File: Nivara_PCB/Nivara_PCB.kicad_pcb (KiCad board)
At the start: 2 copper layers, 102.2 x 83 mm, 20 parts, among them J1 NPN_IN, J10 PNP_OUT, J11 Analog_Out, J2 PNP_IN, J3 D_IN, J4 NPN_OUT, J5 RELAY, J6 RUN/STOP, J7 FUENTE, J8 RS485, J9 Analaog_In, U1 ESP32-S3-WROOM-1, U2 AP63203WU

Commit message: Actualización del pcb
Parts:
- C1: renamed from C3; value C_1206 -> 10uF
- moved C6 28.5 mm to (128.5, 78.7)
- moved R1 26.8 mm to (128.0, 71.3), turned to -90 degrees
- moved C1 13.8 mm to (107.0, 56.5), turned to 180 degrees
- moved C3 13.3 mm to (103.5, 60.0)
- moved C5 9.69 mm to (114.0, 60.0)
- moved C2 9.18 mm to (111.5, 60.0)
- moved U2 8.86 mm to (107.4, 60.0), turned to 180 degrees
- moved L1 3.08 mm to (107.0, 65.5), turned to 0 degrees
- renumbered C4 to C2, C2 to C3, C6 to C5, C1 to C6
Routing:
- net +3.3V: track 0.00 -> 11.8 mm
- net Net-(U2-SW): track 0.00 -> 11.6 mm
- net VCC: track 0.00 -> 10.8 mm
- net Net-(U2-BST): track 0.00 -> 2.73 mm
- net GND: vias 0 -> 17
- added copper zone on F.Cu, net GND

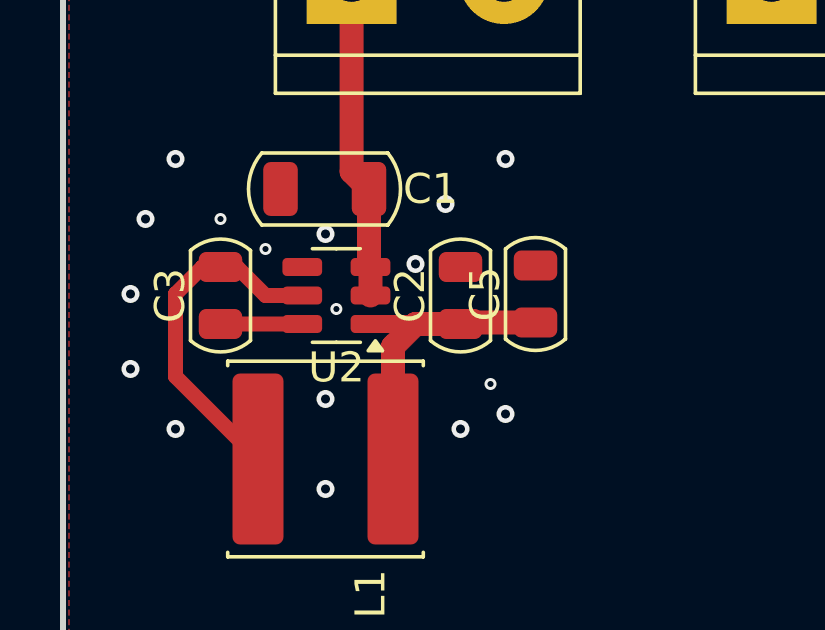
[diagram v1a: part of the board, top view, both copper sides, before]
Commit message: Fuente de 12V para activar optoacopladores y relés
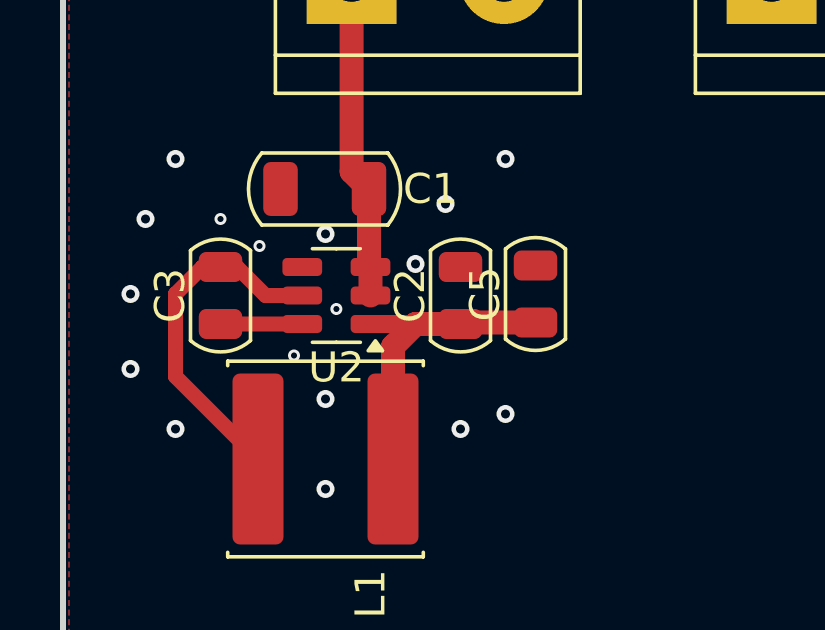
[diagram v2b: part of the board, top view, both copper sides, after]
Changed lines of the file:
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@@
 	)
 	(via
-		(at 112.55 63)
+		(at 106 62.05)
 		(size 0.4)
 		(drill 0.2)
@@
 	)
 	(via
-		(at 105.05 58.5)
+		(at 104.85 58.4)
 		(size 0.4)
 		(drill 0.2)

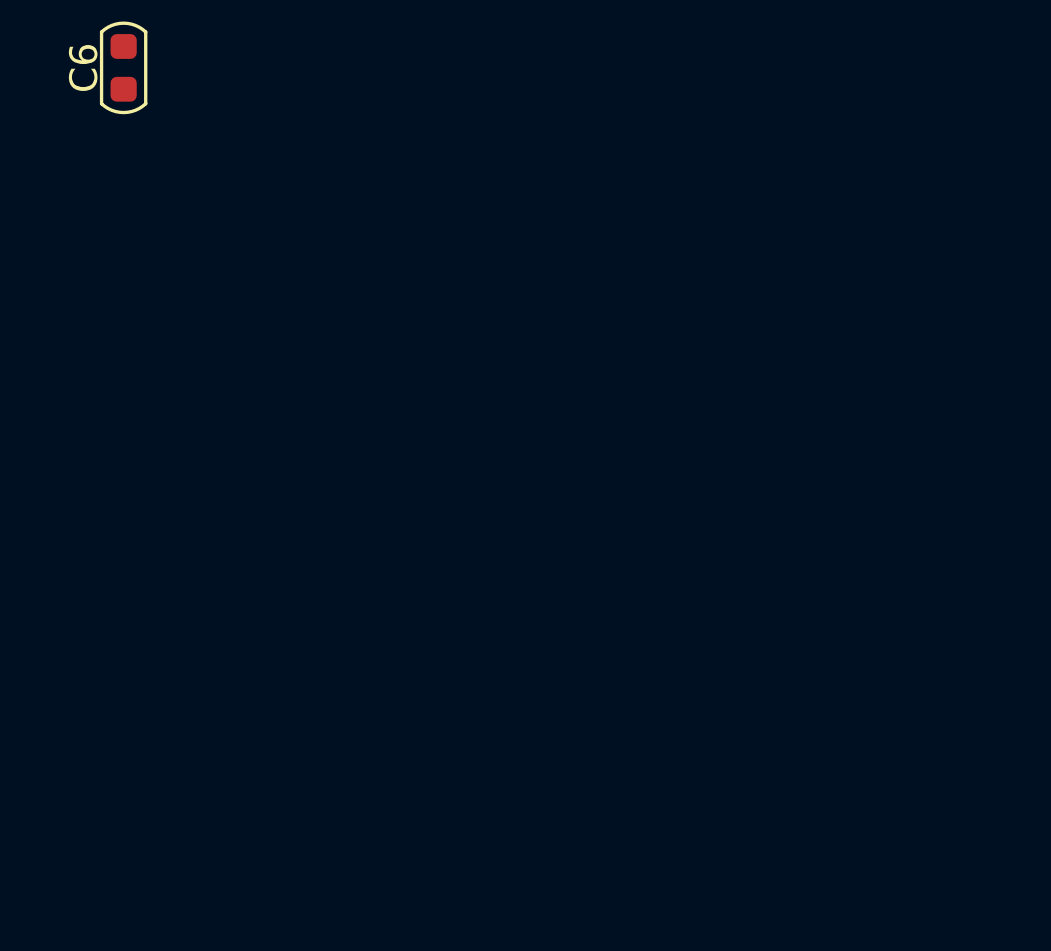
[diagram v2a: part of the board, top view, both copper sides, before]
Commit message: Cambio a fuente de 5V para utilizar reles HF49FD Es mejor utilizar una fuente de 5V para alimentar los reles y los periféricos en general, que 12V
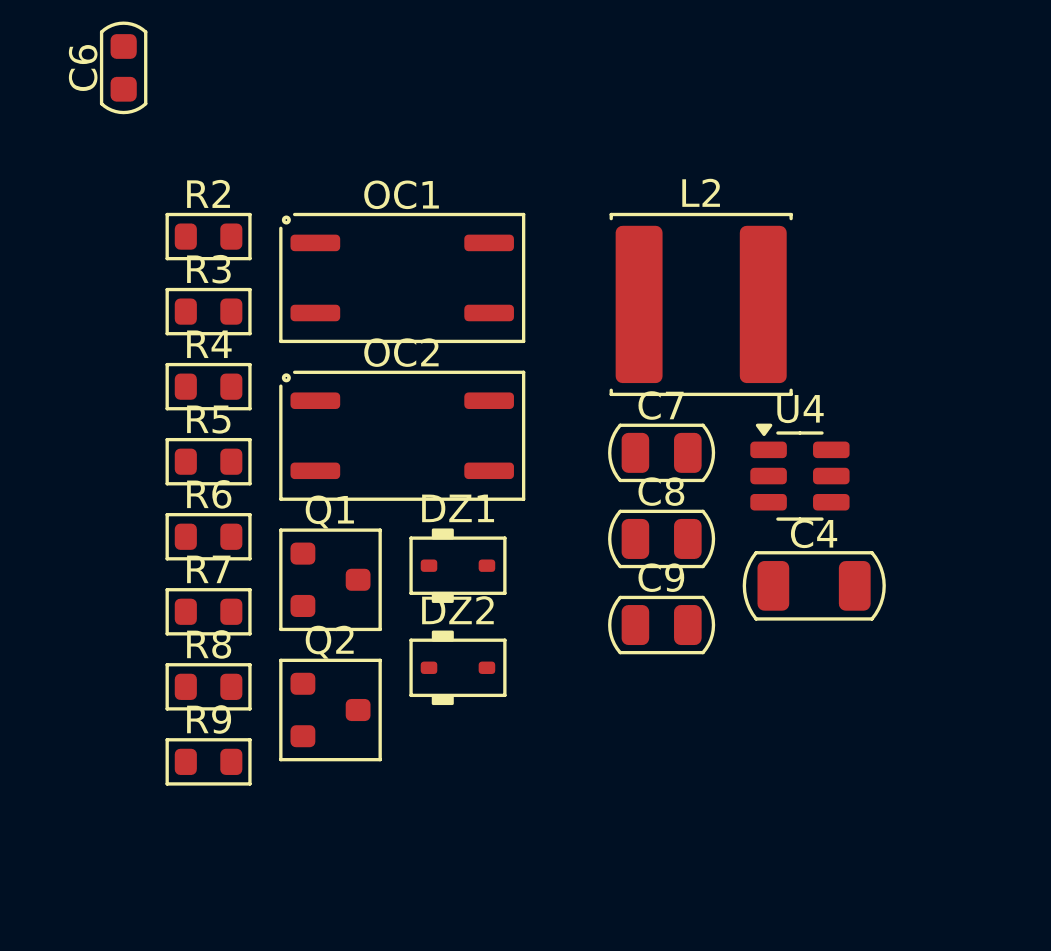
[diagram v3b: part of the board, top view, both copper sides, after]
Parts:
- added C4: 10uF, PCM_Capacitor_SMD_AKL:C_1206_3216Metric, F.Cu at (153.5, 97.5)
- added C7: 100nF, PCM_Capacitor_SMD_AKL:C_0805_2012Metric, F.Cu at (148.0, 92.7)
- added C8: 22uF, PCM_Capacitor_SMD_AKL:C_0805_2012Metric, F.Cu at (148.0, 95.8)
- added C9: 22uF, PCM_Capacitor_SMD_AKL:C_0805_2012Metric, F.Cu at (148.0, 98.9)
- added DZ1: BZT52C10S, PCM_Diode_SMD_AKL:D_SOD-323, F.Cu at (140.6, 96.8)
- added DZ2: BZT52C10S, PCM_Diode_SMD_AKL:D_SOD-323, F.Cu at (140.6, 100.5)
- added L2: 4u7H, Inductor_SMD:L_APV_ANR6028, F.Cu at (149.4, 87.3)
- added OC1: LTV-356T, PCM_Package_SO_AKL:SO-4_4.4x3.9mm_P2.54mm, F.Cu at (138.6, 86.3)
- added OC2: LTV-356T, PCM_Package_SO_AKL:SO-4_4.4x3.9mm_P2.54mm, F.Cu at (138.6, 92.1)
- added Q1: IRLML6344, PCM_Package_TO_SOT_SMD_AKL:SOT-23, F.Cu at (136.0, 97.3)
- added Q2: IRLML6344, PCM_Package_TO_SOT_SMD_AKL:SOT-23, F.Cu at (136.0, 102.0)
- added R2: 7k, PCM_Resistor_SMD_AKL:R_0603_1608Metric, F.Cu at (131.6, 84.8)
- added R3: 7k, PCM_Resistor_SMD_AKL:R_0603_1608Metric, F.Cu at (131.6, 87.6)
- added R4: 1k, PCM_Resistor_SMD_AKL:R_0603_1608Metric, F.Cu at (131.6, 90.3)
- added R5: 10k, PCM_Resistor_SMD_AKL:R_0603_1608Metric, F.Cu at (131.6, 93.0)
- added R6: 1k, PCM_Resistor_SMD_AKL:R_0603_1608Metric, F.Cu at (131.6, 95.7)
- added R7: 10k, PCM_Resistor_SMD_AKL:R_0603_1608Metric, F.Cu at (131.6, 98.4)
- added R8: 22k, PCM_Resistor_SMD_AKL:R_0603_1608Metric, F.Cu at (131.6, 101.2)
- added R9: 22k, PCM_Resistor_SMD_AKL:R_0603_1608Metric, F.Cu at (131.6, 103.9)
- added U4: AP63205WU, Package_TO_SOT_SMD:TSOT-23-6, F.Cu at (153.0, 93.5)
